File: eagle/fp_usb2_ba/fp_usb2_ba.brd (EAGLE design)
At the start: 95 x 24.7 mm, 2 parts

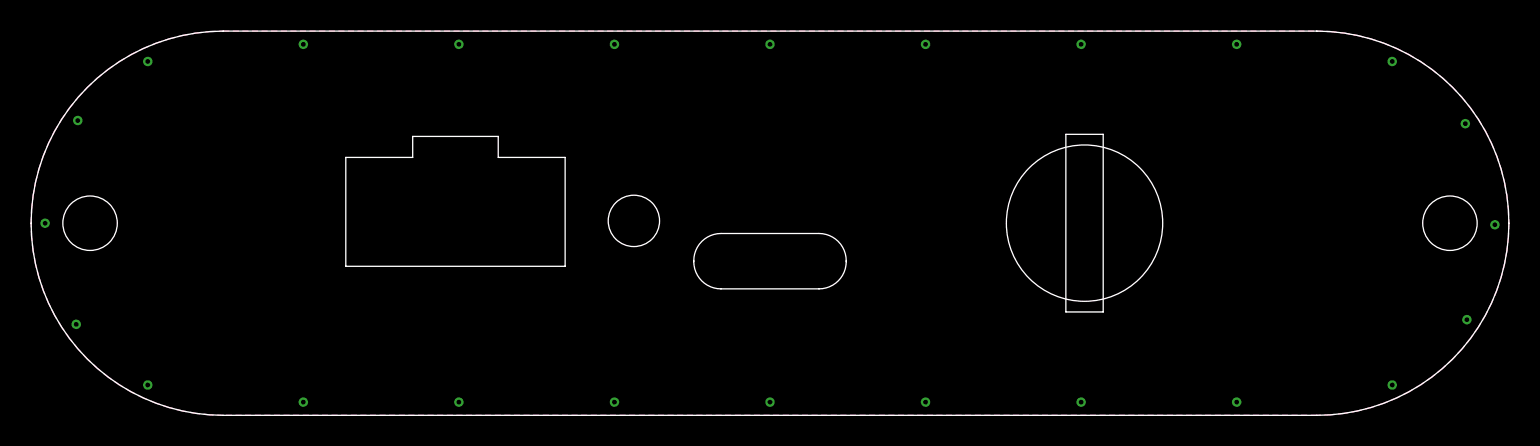
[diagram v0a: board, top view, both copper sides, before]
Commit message: Updates for JS220 first production build.
* Updated back panel for production build.
  * Increased USB hole size by 0.2 mm in left, right, and up directions
  * Bumped rev from C to D.
* Added additional boards:
  * fb_usb2_ba: USB 2.0 B/A connector
  * fp_bnc: BNC & 0.1" headers
  * fp_js110: Safety banana jacks configured like the JS110.
  * fp_baseline: Starting point for creating new boards in Eagle.
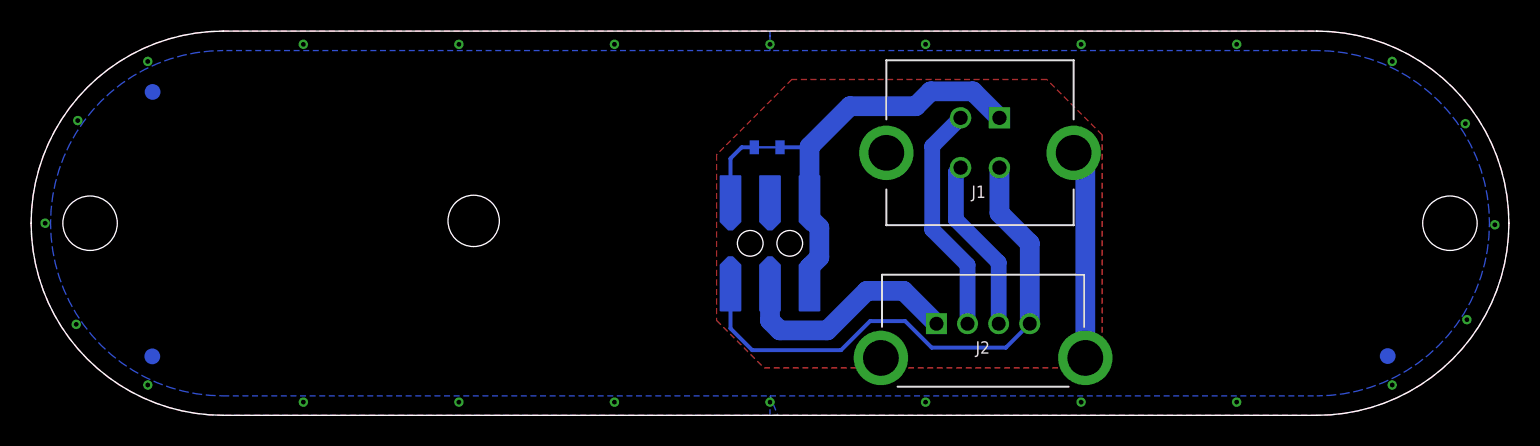
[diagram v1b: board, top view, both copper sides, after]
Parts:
- added FUD1, FUD2, FUD3: FIDUCIAL_1MM, jetperch:FIDUCIAL_1MM_2MM
- added J1: M701-330442, jetperch:USB-B-VTH
- added J2: UJ2-AV-1-TH, jetperch:USB-A-VTH
- added J3: (no value), jetperch:J0603
- added J5: TSM-103-01-S-DV-A, jetperch:CONN_0.1_3X2_MSA
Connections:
- new net D_N: J1.2, J2.2
- new net D_P: J1.3, J2.3
- new net I+: J1.1, J3.2, J5.1, J5.2
- new net I-: J2.1, J5.3, J5.4
- new net SHIELD: J1.SHIELD@1, J1.SHIELD@3, J2.SHIELD@1, J2.SHIELD@3
- new net V+: J3.1, J5.6
- new net V-: J1.4, J2.4, J5.5
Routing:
- net V-: track 0.00 -> 35.7 mm
- net I+: track 0.00 -> 25.6 mm
- net I-: track 0.00 -> 15.3 mm
- net D_N: track 0.00 -> 14.9 mm
- net SHIELD: track 0.00 -> 13.5 mm
- net D_P: track 0.00 -> 11.3 mm
- net V+: track 0.00 -> 4.75 mm
- added copper zone on layer 1, net V-
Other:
- outline, holes or cut-outs redrawn
- board text added: "2x holes"
- board text added: "Device"
- board text added: "Host computer"
- board text added: "JS220_fp_usb2_ba_pcb_a JS220 USB 2.0 B/A Front Panel Rev A"
- board text added: "Sensor Status"
- board text removed: "Controller Status"
- board text removed: "GPIO"
- board text removed: "GPIO and trigger are referenced to USB ground"
- board text removed: "OUT0 GND IN2 IN0 Vref"
- board text removed: "OUT1 GND IN3 IN1 GND"
- board text removed: "Out: 3.3V, 50 Ω In: TTL & 3.3V compatible"
- board text removed: "Trigger"
- board text removed: "USB"
- board text removed: "js220_ep_pcb_revC JS220 End Panel, Rev D 2022 Jetperch LLC"

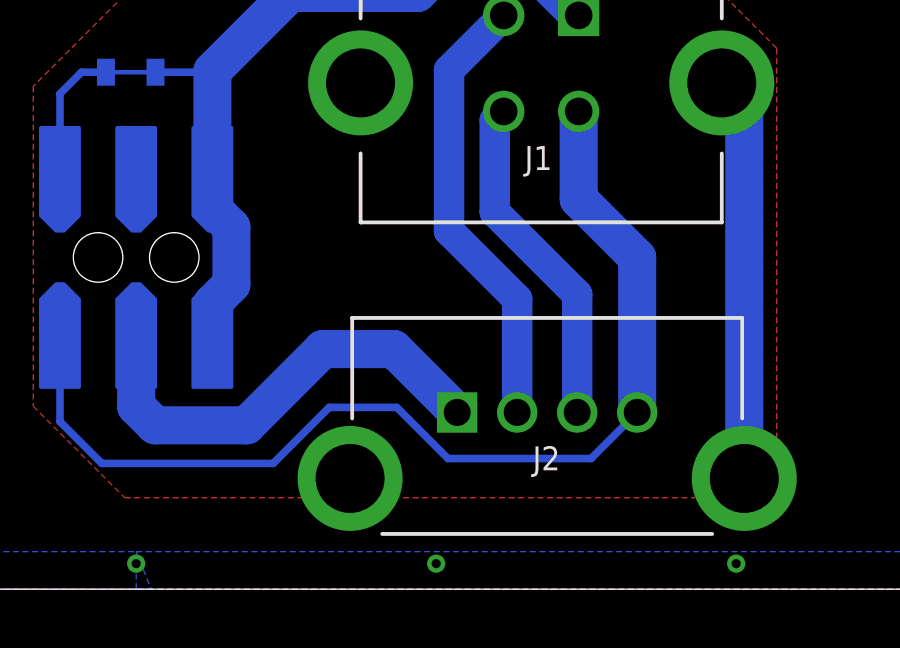
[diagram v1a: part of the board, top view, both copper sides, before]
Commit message: Fixed fb_usb2_ba connector A USB connector holes.
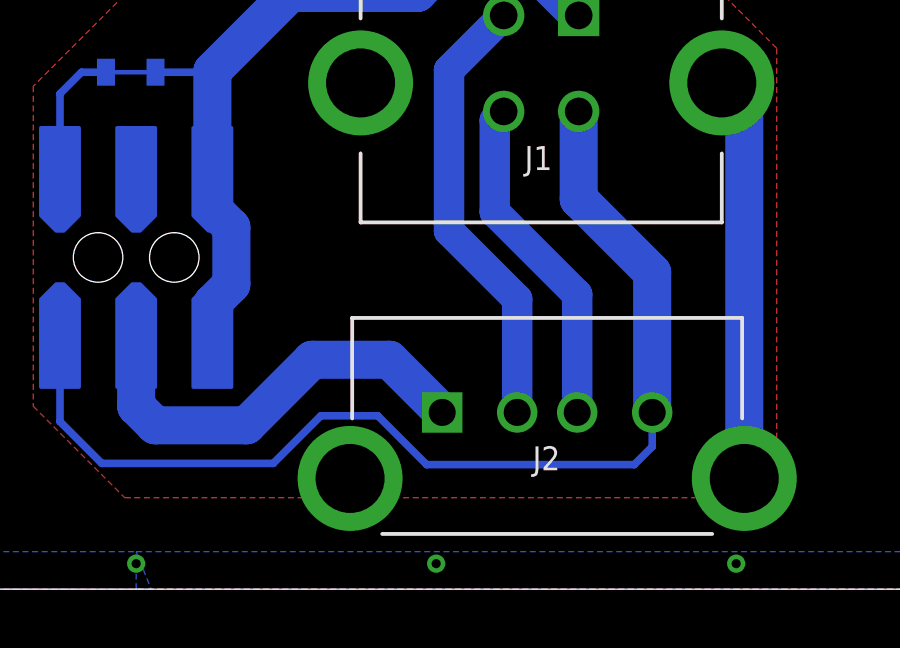
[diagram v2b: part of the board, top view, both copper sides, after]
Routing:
- net V-: track 35.7 -> 37.0 mm
- net I-: track 15.3 -> 14.5 mm
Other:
- board text added: "JS220_fp_usb2_ba_pcb_a JS220 USB 2.0 B/A Front Panel Rev B"
- board text removed: "JS220_fp_usb2_ba_pcb_a JS220 USB 2.0 B/A Front Panel Rev A"
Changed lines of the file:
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@@
 <text x="47.5" y="20.581" size="1.27" layer="26" font="vector" ratio="20" rot="MR0" align="center">JS220_fp_usb2_ba_pcb_a
 JS220 USB 2.0 B/A Front Panel
-Rev A</text>
+Rev B</text>
 <dimension x1="0" y1="12.35" x2="95" y2="12.35" x3="47.5" y3="40.64" textsize="1.778" layer="47" dtype="horizontal"/>
 <dimension x1="12.35" y1="0" x2="12.35" y2="24.7" x3="-17.35" y3="12.35" textsize="1.778" layer="47" dtype="vertical"/>
@@
 <wire x1="44.96" y1="5.586" x2="46.355" y2="4.191" width="0.254" layer="16"/>
 <wire x1="46.355" y1="4.191" x2="52.0668" y2="4.191" width="0.254" layer="16"/>
-<wire x1="52.0668" y1="4.191" x2="53.9338" y2="6.058" width="0.254" layer="16"/>
-<wire x1="53.9338" y1="6.058" x2="56.188" y2="6.058" width="0.254" layer="16"/>
+<wire x1="52.0668" y1="4.191" x2="53.6544" y2="5.7786" width="0.254" layer="16"/>
+<wire x1="53.6544" y1="5.7786" x2="55.553" y2="5.7786" width="0.254" layer="16"/>
 <polygon width="0.254" layer="1" isolate="0.254">
 <vertex x="44.069" y="16.764"/>
@@
 <vertex x="48.895" y="21.59"/>
 </polygon>
-<wire x1="56.188" y1="6.058" x2="57.893" y2="4.353" width="0.254" layer="16"/>
-<wire x1="64.2" y1="5.89" x2="64.2" y2="11.053" width="1.27" layer="16"/>
-<wire x1="64.2" y1="11.053" x2="62.25" y2="13.003" width="1.27" layer="16"/>
+<wire x1="55.553" y1="5.7786" x2="57.1818" y2="4.1498" width="0.254" layer="16"/>
 <wire x1="62.25" y1="13.003" x2="62.25" y2="15.924" width="1.27" layer="16"/>
-<wire x1="62.663" y1="4.353" x2="64.2" y2="5.89" width="0.254" layer="16"/>
-<wire x1="57.893" y1="4.353" x2="62.663" y2="4.353" width="0.254" layer="16"/>
+<wire x1="64.7" y1="4.747" x2="64.7" y2="5.89" width="0.254" layer="16"/>
+<wire x1="64.7" y1="4.747" x2="64.1028" y2="4.1498" width="0.254" layer="16"/>
+<wire x1="57.1818" y1="4.1498" x2="64.1028" y2="4.1498" width="0.254" layer="16"/>
+<wire x1="64.7" y1="5.89" x2="64.7" y2="10.553" width="1.27" layer="16"/>
+<wire x1="64.7" y1="10.553" x2="62.25" y2="13.003" width="1.27" layer="16"/>
 </signal>
 <signal name="I-">
@@
 <wire x1="47.5" y1="6.094" x2="48.133" y2="5.461" width="1.27" layer="16"/>
 <wire x1="48.133" y1="5.461" x2="51.181" y2="5.461" width="1.27" layer="16"/>
-<wire x1="51.181" y1="5.461" x2="53.721" y2="8.001" width="1.27" layer="16"/>
-<wire x1="56.089" y1="8.001" x2="58.2" y2="5.89" width="1.27" layer="16"/>
-<wire x1="53.721" y1="8.001" x2="56.089" y2="8.001" width="1.27" layer="16"/>
+<wire x1="51.181" y1="5.461" x2="53.3654" y2="7.6454" width="1.27" layer="16"/>
+<wire x1="55.9446" y1="7.6454" x2="57.7" y2="5.89" width="1.27" layer="16"/>
+<wire x1="53.3654" y1="7.6454" x2="55.9446" y2="7.6454" width="1.27" layer="16"/>
 <wire x1="47.5" y1="8.5165" x2="47.5" y2="13.5965" width="0" layer="19" extent="16-16"/>
 </signal>
